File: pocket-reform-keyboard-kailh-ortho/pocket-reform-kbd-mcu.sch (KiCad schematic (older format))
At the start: 29 parts, among them J1 USB, J2 UART, J3 AUX, SW61 RESET, U1 ATMEGA32U4-AU, U1 MCP1700-3302E_SOT23, Y1 16MHz

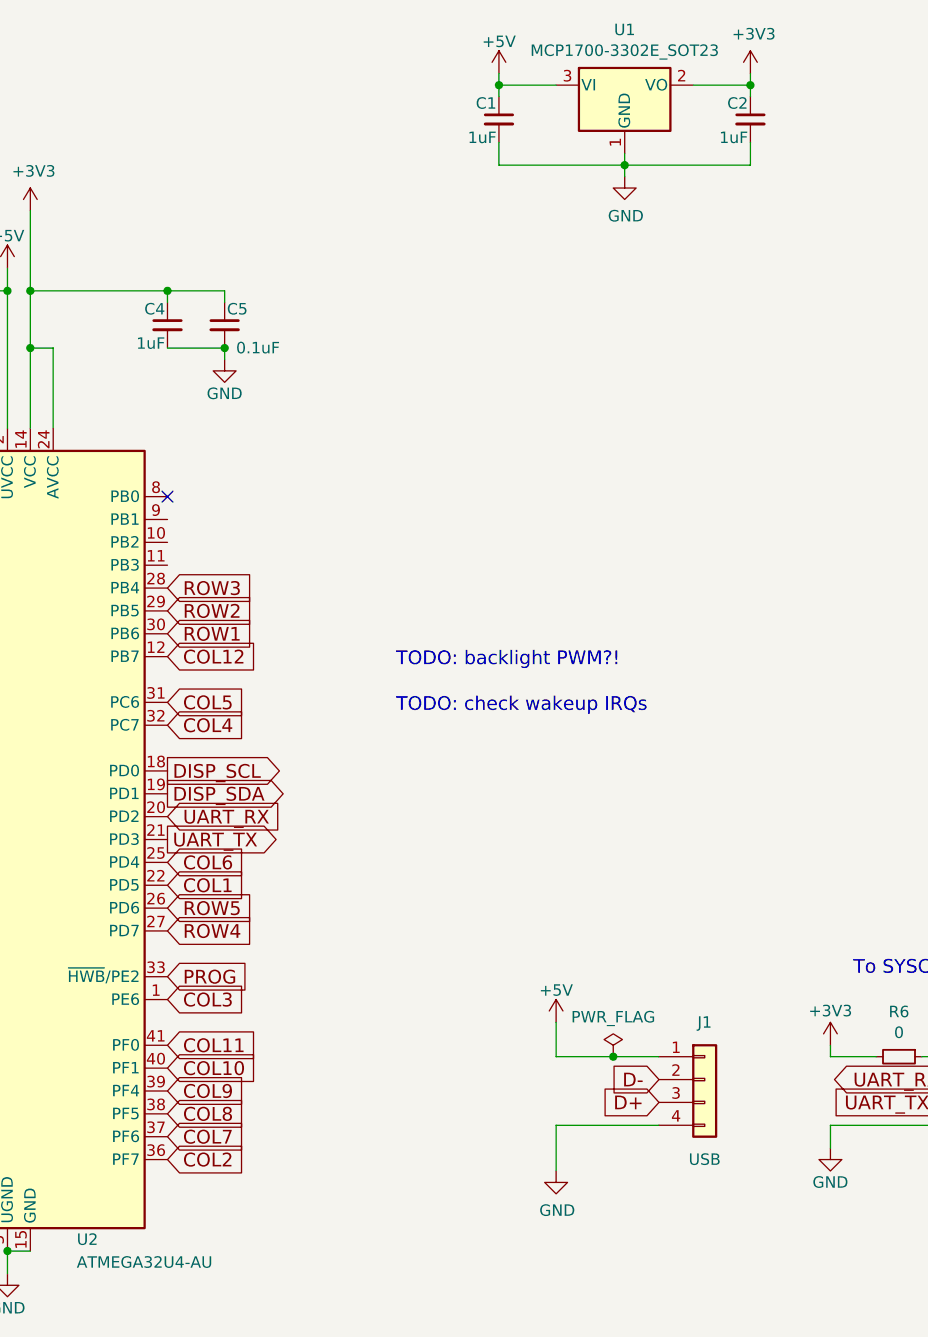
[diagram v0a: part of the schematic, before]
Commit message: keyboard: tweak trackball mount, wire up tb buttons and leds
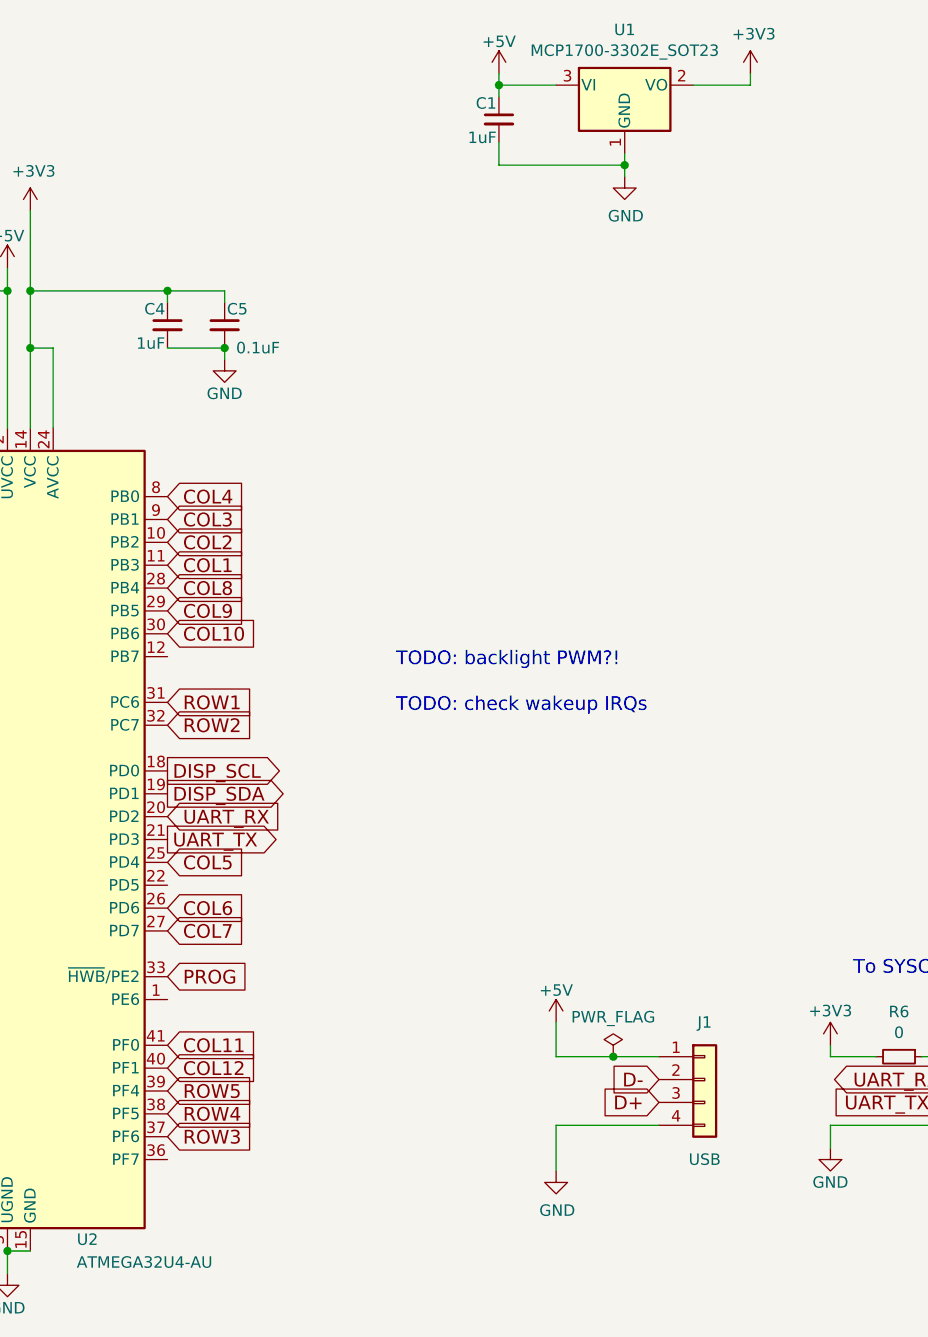
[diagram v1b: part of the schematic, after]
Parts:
- removed C2: 1uF, Capacitor_SMD:C_0603_1608Metric, symbol Device:C_Small
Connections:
- net COL1: now also U1.11 (PB3); no longer U1.22 (PD5)
- net COL10: now also U1.30 (PB6); no longer U1.40 (PF1)
- net COL12: now also U1.40 (PF1); no longer U1.12 (PB7)
- net COL2: now also U1.10 (PB2); no longer U1.36 (PF7)
- net COL3: now also U1.9 (PB1); no longer U1.1 (PE6)
- net COL4: now also U1.8 (PB0); no longer U1.32 (PC7)
- net COL5: now also U1.25 (PD4); no longer U1.31 (PC6)
- net COL6: now also U1.26 (PD6); no longer U1.25 (PD4)
- net COL7: now also U1.27 (PD7); no longer U1.37 (PF6)
- net COL8: now also U1.28 (PB4); no longer U1.38 (PF5)
- net COL9: now also U1.29 (PB5); no longer U1.39 (PF4)
- net ROW1: now also U1.31 (PC6); no longer U1.30 (PB6)
- net ROW2: now also U1.32 (PC7); no longer U1.29 (PB5)
- net ROW3: now also U1.37 (PF6); no longer U1.28 (PB4)
- net ROW4: now also U1.38 (PF5); no longer U1.27 (PD7)
- net ROW5: now also U1.39 (PF4); no longer U1.26 (PD6)
- no-connect marks 1 -> 0
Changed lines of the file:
@@
 Text GLabel 2950 3100 0    60   Input ~ 0
 RESET
-Text GLabel 4450 3700 2    60   Input ~ 0
+Text GLabel 4450 4000 2    60   Input ~ 0
 ROW1
-Text GLabel 4450 3600 2    60   Input ~ 0
+Text GLabel 4450 4100 2    60   Input ~ 0
 ROW2
+Text GLabel 4450 5900 2    60   Input ~ 0
+ROW3
+Text GLabel 4450 5800 2    60   Input ~ 0
+ROW4
+Text GLabel 4450 5700 2    60   Input ~ 0
+ROW5
+Text GLabel 4450 3400 2    60   Input ~ 0
+COL1
+Text GLabel 4450 3300 2    60   Input ~ 0
+COL2
+Text GLabel 4450 3200 2    60   Input ~ 0
+COL3
+Text GLabel 4450 3100 2    60   Input ~ 0
+COL4
+Text GLabel 4450 4700 2    60   Input ~ 0
+COL5
+Text GLabel 4450 4900 2    60   Input ~ 0
+COL6
+Text GLabel 4450 5000 2    60   Input ~ 0
+COL7
 Text GLabel 4450 3500 2    60   Input ~ 0
-ROW3
-Text GLabel 4450 5000 2    60   Input ~ 0
-ROW4
-Text GLabel 4450 4900 2    60   Input ~ 0
-ROW5
-Text GLabel 4450 4800 2    60   Input ~ 0
-COL1
-Text GLabel 4450 6000 2    60   Input ~ 0
-COL2
-Text GLabel 4450 5300 2    60   Input ~ 0
-COL3
-Text GLabel 4450 4100 2    60   Input ~ 0
-COL4
-Text GLabel 4450 4000 2    60   Input ~ 0
-COL5
-Text GLabel 4450 4700 2    60   Input ~ 0
-COL6
-Text GLabel 4450 5900 2    60   Input ~ 0
-COL7
-Text GLabel 4450 5800 2    60   Input ~ 0
 COL8
-Text GLabel 4450 5700 2    60   Input ~ 0
-COL9
-Text GLabel 4450 5600 2    60   Input ~ 0
-COL10
 Text GLabel 4450 5500 2    60   Input ~ 0
 COL11
@@
 	-1   0    0    -1
 $EndComp
-$Comp
-L Device:C_Small C2
-U 1 1 5F223065
-P 7000 1450
-F 0 "C2" H 7010 1520 50  0000 L CNN
-F 1 "1uF" H 7010 1370 50  0000 L CNN
-F 2 "Capacitor_SMD:C_0603_1608Metric" H 7000 1450 50  0001 C CNN
-F 3 "" H 7000 1450 50  0001 C CNN
-F 4 "TDK" H 7000 1450 50  0001 C CNN "Manufacturer"
-F 5 "C1608X8L1C105K080AC" H 7000 1450 50  0001 C CNN "Manufacturer_No"
-F 6 "" H 7000 1450 50  0001 C CNN "Flags"
-	1    7000 1450
-	-1   0    0    -1
-$EndComp
-Wire Wire Line
-	7000 1350 7000 1300
-Connection ~ 7000 1300
 Wire Wire Line
 	5900 1300 5900 1350
@@
 Wire Wire Line
 	6450 1650 6450 1700
-Wire Wire Line
-	6450 1650 7000 1650
-Wire Wire Line
-	7000 1650 7000 1550
 Wire Wire Line
 	6150 5850 6600 5850
@@
 Wire Wire Line
 	1550 2200 1700 2200
-NoConn ~ 4450 3100
 $Comp
 L reform2-keyboard-rescue:ATmega32U4-AU-MCU_Microchip_ATmega U1
@@
 	1    0    0    -1
 $EndComp
-Text GLabel 4450 3800 2    60   Input ~ 0
+Text GLabel 4450 5600 2    60   Input ~ 0
 COL12
 Text Notes 5450 4050 0    60   ~ 0
@@
 Text Notes 5450 3850 0    60   ~ 0
 TODO: backlight PWM?!
+Text GLabel 4450 3600 2    60   Input ~ 0
+COL9
+Text GLabel 4450 3700 2    60   Input ~ 0
+COL10
 $EndSCHEMATC
